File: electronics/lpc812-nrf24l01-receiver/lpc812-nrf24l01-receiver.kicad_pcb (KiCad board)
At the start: 2 copper layers, 25 x 29 mm, 21 parts, among them K1 BAT, K2 CH3, K3 TH, K4 ST, P1 NRF24L01+, SW1 ISP/BIND, U1 MCP1703, U2 LPC812, X1 16MHz

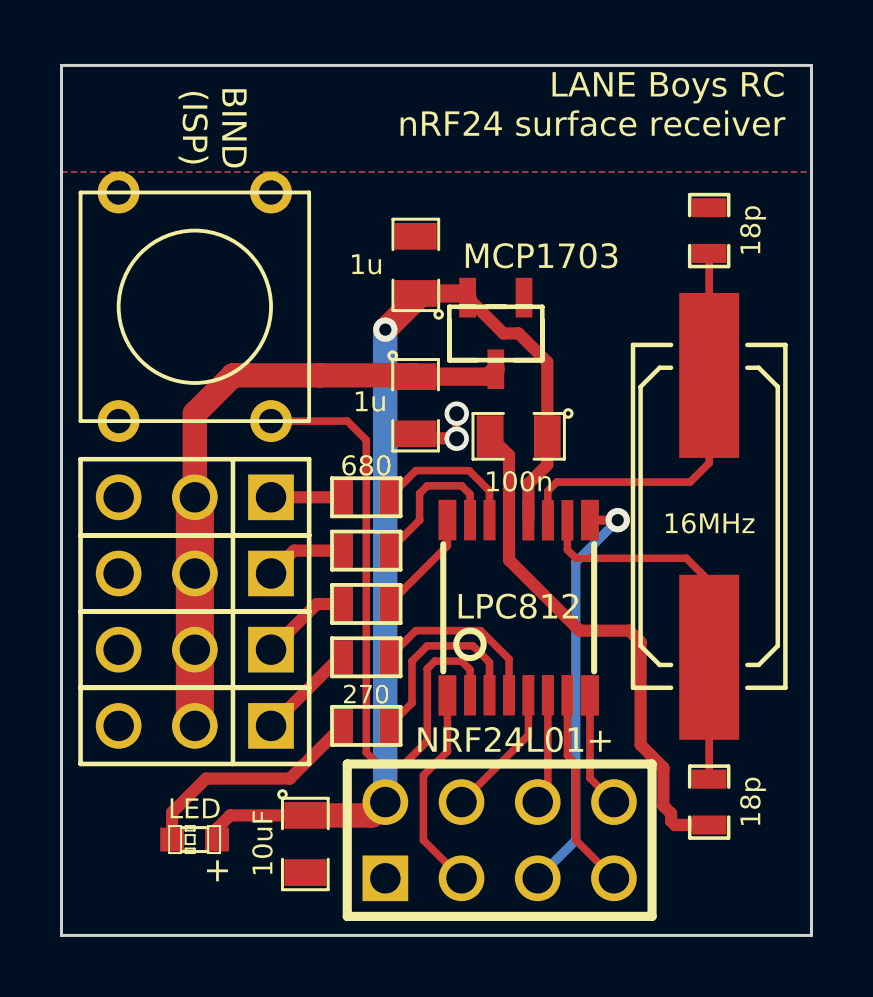
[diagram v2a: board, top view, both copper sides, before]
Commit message: Use Multicomp switches we have. Rename library to proper name
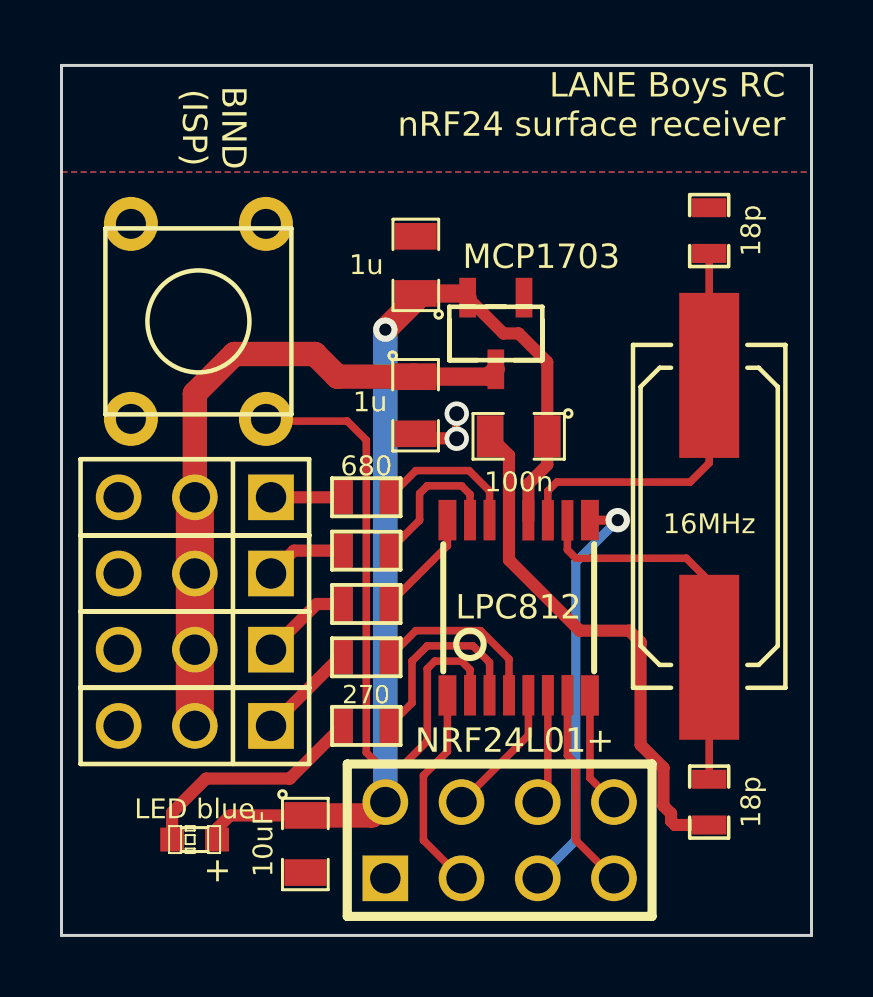
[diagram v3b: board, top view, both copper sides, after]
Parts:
- D1: value LED -> LED blue
- SW1: value ISP/BIND -> BIND/ISP; footprint SW_PUSH_SMALL -> MCDTS6
- moved SW1 0.50 mm to (67.6, 65.5)
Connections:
- SW1 pad 1: /ISP-BIND -> (no net)
- SW1 pad 2: VSS -> /ISP-BIND
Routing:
- net +BATT: track 21.1 -> 22.1 mm
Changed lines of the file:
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@@
 (kicad_pcb (version 3) (host pcbnew "(2013-jul-07)-stable")
   (general
-    (links 47)
-    (no_connects 1)
+    (links 46)
+    (no_connects 0)
     (area 62.949999 56.949999 88.050001 86.050001)
     (thickness 1.6)
     (drawings 16)
-    (tracks 126)
+    (tracks 127)
     (zones 0)
     (modules 21)
@@
   )
   (setup
-    (last_trace_width 0.254)
+    (last_trace_width 1)
     (user_trace_width 0.2032)
     (user_trace_width 0.254)
@@
   (net 15 /XTALIN)
   (net 16 /XTALOUT)
-  (net 17 N-0000010)
-  (net 18 N-0000011)
-  (net 19 N-0000012)
-  (net 20 N-000007)
+  (net 17 N-000001)
+  (net 18 N-0000010)
+  (net 19 N-0000011)
+  (net 20 N-000008)
   (net 21 N-000009)
   (net 22 VSS)
@@
     (add_net /XTALIN)
     (add_net /XTALOUT)
+    (add_net N-000001)
     (add_net N-0000010)
     (add_net N-0000011)
-    (add_net N-0000012)
-    (add_net N-000007)
+    (add_net N-000008)
     (add_net N-000009)
     (add_net VSS)
@@
     (pad 1 thru_hole rect (at -2.54 0 180) (size 1.524 1.524) (drill 1.016)
       (layers *.Cu *.Mask F.SilkS)
-      (net 19 N-0000012)
+      (net 19 N-0000011)
     )
     (pad 2 thru_hole circle (at 0 0 180) (size 1.524 1.524) (drill 1.016)
@@
     (pad 1 thru_hole rect (at -2.54 0 180) (size 1.524 1.524) (drill 1.016)
       (layers *.Cu *.Mask F.SilkS)
-      (net 18 N-0000011)
+      (net 18 N-0000010)
     )
     (pad 2 thru_hole circle (at 0 0 180) (size 1.524 1.524) (drill 1.016)
@@
     (pad 1 thru_hole rect (at -2.54 0 180) (size 1.524 1.524) (drill 1.016)
       (layers *.Cu *.Mask F.SilkS)
-      (net 17 N-0000010)
+      (net 20 N-000008)
     )
     (pad 2 thru_hole circle (at 0 0 180) (size 1.524 1.524) (drill 1.016)
@@
       (effects (font (size 0.508 0.508) (thickness 0.127)))
     )
-    (fp_text value LED (at 0 1.016 180) (layer F.SilkS)
+    (fp_text value "LED blue" (at 0 1.016 180) (layer F.SilkS)
       (effects (font (size 0.6604 0.6604) (thickness 0.1524)))
     )
@@
     (pad 2 smd rect (at 0.7493 0 180) (size 0.79756 0.79756)
       (layers F.Cu F.Paste F.Mask)
-      (net 20 N-000007)
-    )
-  )
-  (module SW_PUSH_SMALL (layer F.Cu)
-    (at 67.445 65.045 270)
-    (fp_text reference SW1 (at 0 -0.762 270) (layer F.SilkS) hide
-      (effects (font (size 1.016 1.016) (thickness 0.2032)))
-    )
-    (fp_text value ISP/BIND (at -0.127 -0.127 360) (layer F.SilkS) hide
-      (effects (font (size 0.8128 0.8128) (thickness 0.1778)))
-    )
-    (fp_circle (center 0 0) (end 0 -2.54) (layer F.SilkS) (width 0.127))
-    (fp_line (start -3.81 -3.81) (end 3.81 -3.81) (layer F.SilkS) (width 0.127))
-    (fp_line (start 3.81 -3.81) (end 3.81 3.81) (layer F.SilkS) (width 0.127))
-    (fp_line (start 3.81 3.81) (end -3.81 3.81) (layer F.SilkS) (width 0.127))
-    (fp_line (start -3.81 -3.81) (end -3.81 3.81) (layer F.SilkS) (width 0.127))
-    (pad 1 thru_hole circle (at 3.81 -2.54 270) (size 1.397 1.397) (drill 0.8128)
-      (layers *.Cu *.Mask F.SilkS)
-      (net 9 /ISP-BIND)
-    )
-    (pad 2 thru_hole circle (at 3.81 2.54 270) (size 1.397 1.397) (drill 0.8128)
-      (layers *.Cu *.Mask F.SilkS)
-      (net 22 VSS)
-    )
-    (pad 1 thru_hole circle (at -3.81 -2.54 270) (size 1.397 1.397) (drill 0.8128)
-      (layers *.Cu *.Mask F.SilkS)
-      (net 9 /ISP-BIND)
-    )
-    (pad 2 thru_hole circle (at -3.81 2.54 270) (size 1.397 1.397) (drill 0.8128)
-      (layers *.Cu *.Mask F.SilkS)
-      (net 22 VSS)
+      (net 17 N-000001)
     )
   )
@@
     (pad 2 smd rect (at 0.762 0 180) (size 0.635 1.143)
       (layers F.Cu F.Paste F.Mask)
-      (net 19 N-0000012)
+      (net 19 N-0000011)
     )
     (model smd\resistors\R0603.wrl
@@
     (pad 2 smd rect (at 0.762 0 180) (size 0.635 1.143)
       (layers F.Cu F.Paste F.Mask)
-      (net 18 N-0000011)
+      (net 18 N-0000010)
     )
     (model smd\resistors\R0603.wrl
@@
     (pad 2 smd rect (at 0.762 0 180) (size 0.635 1.143)
       (layers F.Cu F.Paste F.Mask)
-      (net 17 N-0000010)
+      (net 20 N-000008)
     )
     (model smd\resistors\R0603.wrl
@@
     (pad 1 smd rect (at -0.762 0) (size 0.635 1.143)
       (layers F.Cu F.Paste F.Mask)
-      (net 20 N-000007)
+      (net 17 N-000001)
     )
     (pad 2 smd rect (at 0.762 0) (size 0.635 1.143)
@@
     )
   )
+  (module MCDTS6 (layer F.Cu)
+    (at 67.564 65.532 270)
+    (descr "Multicomp MCDTS Series tact switch")
+    (tags "tact switch push button sw spst")
+    (fp_text reference SW1 (at 0 -4 270) (layer F.SilkS) hide
+      (effects (font (size 0.8128 0.8128) (thickness 0.1778)))
+    )
+    (fp_text value BIND/ISP (at 0 4 270) (layer F.SilkS) hide
+      (effects (font (size 0.8128 0.8128) (thickness 0.1778)))
+    )
+    (fp_circle (center 0 0) (end 1.7 0) (layer F.SilkS) (width 0.15))
+    (fp_line (start -3.1 -3.1) (end 3.1 -3.1) (layer F.SilkS) (width 0.15))
+    (fp_line (start 3.1 -3.1) (end 3.1 3.1) (layer F.SilkS) (width 0.15))
+    (fp_line (start 3.1 3.1) (end -3.1 3.1) (layer F.SilkS) (width 0.15))
+    (fp_line (start -3.1 3.1) (end -3.1 -3.1) (layer F.SilkS) (width 0.15))
+    (pad 1 thru_hole circle (at -3.25 -2.25 270) (size 1.8 1.8) (drill 1)
+      (layers *.Cu *.Mask F.SilkS)
+    )
+    (pad 2 thru_hole circle (at 3.25 -2.25 270) (size 1.8 1.8) (drill 1)
+      (layers *.Cu *.Mask F.SilkS)
+      (net 9 /ISP-BIND)
+    )
+    (pad 3 thru_hole circle (at -3.25 2.25 270) (size 1.8 1.8) (drill 1)
+      (layers *.Cu *.Mask F.SilkS)
+      (net 22 VSS)
+    )
+    (pad 4 thru_hole circle (at 3.25 2.25 270) (size 1.8 1.8) (drill 1)
+      (layers *.Cu *.Mask F.SilkS)
+      (net 22 VSS)
+    )
+  )
   (gr_text "BIND\n(ISP)" (at 68.08 59.076 270) (layer F.SilkS)
     (effects (font (size 0.8128 0.8128) (thickness 0.1778)))
@@
   (segment (start 78.56258 70.94542) (end 79.1925 70.3155) (width 0.4064) (layer F.Cu) (net 1))
   (segment (start 79.1925 70.3155) (end 79.1925 69.363) (width 0.4064) (layer F.Cu) (net 1) (status 20))
+  (segment (start 68.764 66.618) (end 71.444 66.618) (width 0.8128) (layer F.Cu) (net 2))
+  (segment (start 67.445 71.395) (end 67.445 67.937) (width 0.8128) (layer F.Cu) (net 2) (status 400010))
+  (segment (start 67.445 67.937) (end 68.764 66.618) (width 0.8128) (layer F.Cu) (net 2))
+  (segment (start 72.1995 67.3735) (end 74.803 67.3735) (width 0.8128) (layer F.Cu) (net 2) (status 800000))
+  (segment (start 71.444 66.618) (end 72.1995 67.3735) (width 0.8128) (layer F.Cu) (net 2))
   (segment (start 74.803 67.3735) (end 77.2323 67.3735) (width 0.6096) (layer F.Cu) (net 2) (status 30))
   (segment (start 77.2323 67.3735) (end 77.478 67.1278) (width 0.6096) (layer F.Cu) (net 2) (status 30))
-  (segment (start 71.628 67.331) (end 74.7605 67.331) (width 0.8128) (layer F.Cu) (net 2) (status 20))
   (segment (start 74.7605 67.331) (end 74.803 67.3735) (width 0.8128) (layer F.Cu) (net 2) (status 30))
-  (segment (start 68.715 67.331) (end 71.628 67.331) (width 0.8128) (layer F.Cu) (net 2))
-  (segment (start 67.445 68.601) (end 68.715 67.331) (width 0.8128) (layer F.Cu) (net 2))
-  (segment (start 67.445 71.395) (end 67.445 68.601) (width 0.8128) (layer F.Cu) (net 2) (status 10))
   (segment (start 67.445 73.935) (end 67.445 71.395) (width 1.27) (layer F.Cu) (net 2) (status 30))
   (segment (start 67.445 76.475) (end 67.445 73.935) (width 1.27) (layer F.Cu) (net 2) (status 30))
@@
   (segment (start 80.145 73.427) (end 83.828 73.427) (width 0.254) (layer F.Cu) (net 16))
   (segment (start 79.86306 73.14506) (end 80.145 73.427) (width 0.254) (layer F.Cu) (net 16))
-  (segment (start 69.985 71.395) (end 72.398 71.395) (width 0.4064) (layer F.Cu) (net 17) (status 30))
+  (segment (start 72.398 79.015) (end 72.369 79.015) (width 0.4064) (layer F.Cu) (net 17) (status 30))
+  (segment (start 72.369 79.015) (end 70.612 80.772) (width 0.4064) (layer F.Cu) (net 17) (status 10))
+  (segment (start 70.612 80.772) (end 67.818 80.772) (width 0.4064) (layer F.Cu) (net 17))
+  (segment (start 67.818 80.772) (end 66.6877 81.9023) (width 0.4064) (layer F.Cu) (net 17))
+  (segment (start 66.6877 81.9023) (end 66.6877 82.804) (width 0.4064) (layer F.Cu) (net 17) (status 20))
   (segment (start 72.398 74.951) (end 71.509 74.951) (width 0.4064) (layer F.Cu) (net 18) (status 10))
   (segment (start 71.509 74.951) (end 69.985 76.475) (width 0.4064) (layer F.Cu) (net 18) (status 20))
   (segment (start 72.398 76.729) (end 72.271 76.729) (width 0.4064) (layer F.Cu) (net 19) (status 30))
   (segment (start 72.271 76.729) (end 69.985 79.015) (width 0.4064) (layer F.Cu) (net 19) (status 30))
-  (segment (start 72.398 79.015) (end 72.369 79.015) (width 0.4064) (layer F.Cu) (net 20) (status 30))
-  (segment (start 72.369 79.015) (end 70.612 80.772) (width 0.4064) (layer F.Cu) (net 20) (status 10))
-  (segment (start 70.612 80.772) (end 67.818 80.772) (width 0.4064) (layer F.Cu) (net 20))
-  (segment (start 67.818 80.772) (end 66.6877 81.9023) (width 0.4064) (layer F.Cu) (net 20))
-  (segment (start 66.6877 81.9023) (end 66.6877 82.804) (width 0.4064) (layer F.Cu) (net 20) (status 20))
+  (segment (start 69.985 71.395) (end 72.398 71.395) (width 0.4064) (layer F.Cu) (net 20) (status 30))
   (segment (start 72.398 73.173) (end 70.747 73.173) (width 0.4064) (layer F.Cu) (net 21) (status 30))
   (segment (start 70.747 73.173) (end 69.985 73.935) (width 0.4064) (layer F.Cu) (net 21) (status 30))

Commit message: Tweak silkscreen of LED
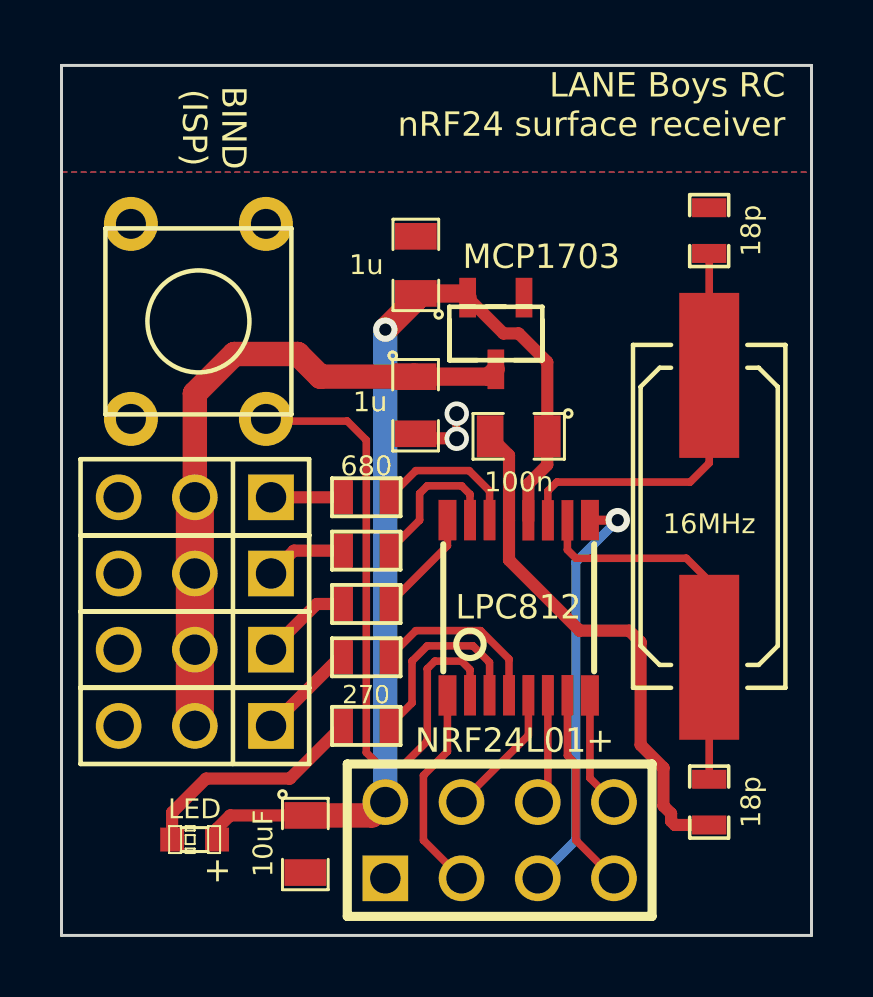
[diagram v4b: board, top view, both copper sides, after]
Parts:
- D1: value LED blue -> LED
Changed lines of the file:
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@@
     (links 46)
     (no_connects 0)
-    (area 62.949999 56.949999 88.050001 86.050001)
+    (area 62.8655 56.949999 88.050001 86.050001)
     (thickness 1.6)
     (drawings 16)
@@
   )
   (setup
-    (last_trace_width 1)
+    (last_trace_width 0.254)
     (user_trace_width 0.2032)
     (user_trace_width 0.254)
@@
       (effects (font (size 0.508 0.508) (thickness 0.127)))
     )
-    (fp_text value "LED blue" (at 0 1.016 180) (layer F.SilkS)
+    (fp_text value LED (at 0 1.016 180) (layer F.SilkS)
       (effects (font (size 0.6604 0.6604) (thickness 0.1524)))
     )
@@
   (segment (start 78.56258 70.94542) (end 79.1925 70.3155) (width 0.4064) (layer F.Cu) (net 1))
   (segment (start 79.1925 70.3155) (end 79.1925 69.363) (width 0.4064) (layer F.Cu) (net 1) (status 20))
-  (segment (start 68.764 66.618) (end 71.444 66.618) (width 0.8128) (layer F.Cu) (net 2))
-  (segment (start 67.445 71.395) (end 67.445 67.937) (width 0.8128) (layer F.Cu) (net 2) (status 400010))
+  (segment (start 68.764 66.618) (end 70.8725 66.618) (width 0.8128) (layer F.Cu) (net 2))
+  (segment (start 67.445 71.395) (end 67.445 67.937) (width 0.8128) (layer F.Cu) (net 2) (status 10))
   (segment (start 67.445 67.937) (end 68.764 66.618) (width 0.8128) (layer F.Cu) (net 2))
-  (segment (start 72.1995 67.3735) (end 74.803 67.3735) (width 0.8128) (layer F.Cu) (net 2) (status 800000))
-  (segment (start 71.444 66.618) (end 72.1995 67.3735) (width 0.8128) (layer F.Cu) (net 2))
+  (segment (start 71.628 67.3735) (end 74.803 67.3735) (width 0.8128) (layer F.Cu) (net 2) (status 800000))
+  (segment (start 70.8725 66.618) (end 71.628 67.3735) (width 0.8128) (layer F.Cu) (net 2))
   (segment (start 74.803 67.3735) (end 77.2323 67.3735) (width 0.6096) (layer F.Cu) (net 2) (status 30))
   (segment (start 77.2323 67.3735) (end 77.478 67.1278) (width 0.6096) (layer F.Cu) (net 2) (status 30))

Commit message: Change components to 0805 which we have in stock
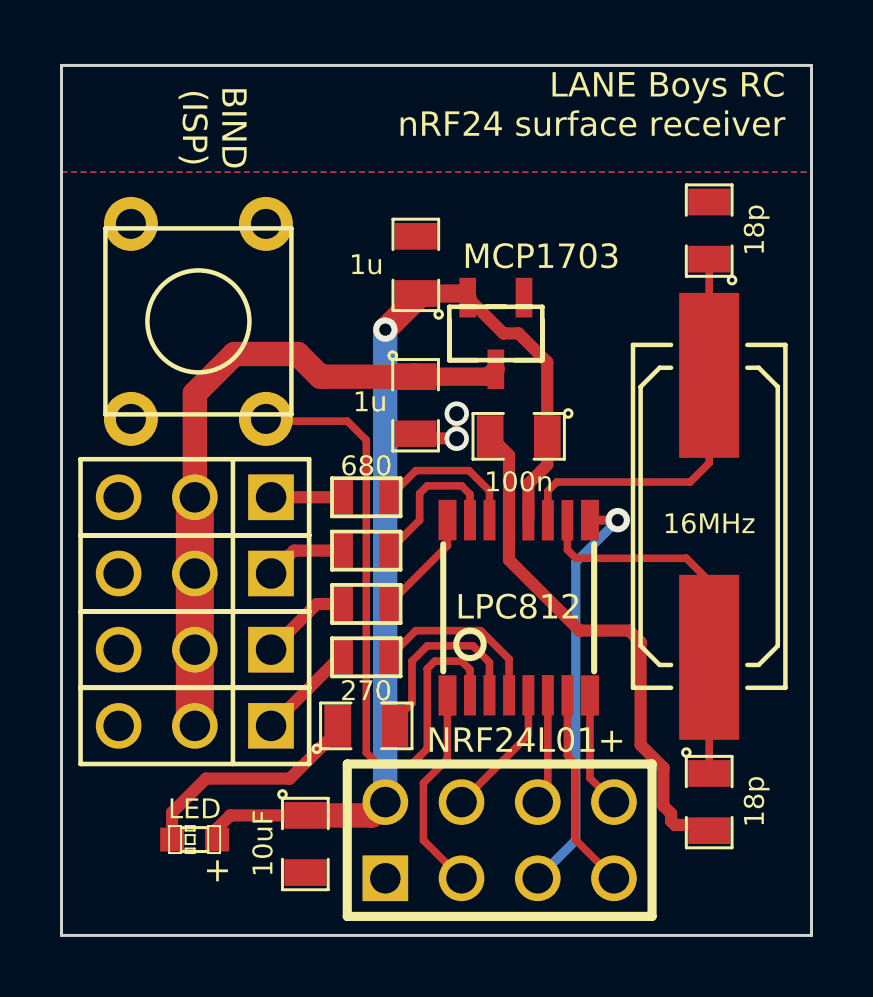
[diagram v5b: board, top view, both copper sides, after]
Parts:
- C4, C5: footprint SM0603_Capa -> SM0805
- R1: footprint SM0603 -> SM0805
